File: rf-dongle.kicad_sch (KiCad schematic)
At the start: 0 parts

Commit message: add first draft of schematic
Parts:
- added C1, C17, C18, C2: 12pF, Capacitor_SMD:C_0402_1005Metric, symbol Device:C
- added C10, C13, C22: N.C., Capacitor_SMD:C_0402_1005Metric, symbol Device:C
- added C11: 100pF, Capacitor_SMD:C_0402_1005Metric, symbol Device:C
- added C12, C23, C5, C7, C8: 100nF, Capacitor_SMD:C_0402_1005Metric, symbol Device:C
- added C14, C15: 1.0µF, Capacitor_SMD:C_0603_1608Metric, symbol Device:C
- added C19, C20, C6: 4.7µF, Capacitor_SMD:C_0603_1608Metric, symbol Device:C
- added C3: 0.8pF, Capacitor_SMD:C_0402_1005Metric, symbol Device:C
- added C4: 0.5pF, Capacitor_SMD:C_0402_1005Metric, symbol Device:C
- added C9: 820pF, Capacitor_SMD:C_0402_1005Metric, symbol Device:C
- added D1: PRTR5V0U2X, Package_TO_SOT_SMD:SOT-143, symbol Power_Protection:PRTR5V0U2X
- added D2, D3: LED, LED_SMD:LED_0402_1005Metric, symbol Device:LED
- added J1: USB_A, 1_Library:PCB_USB_connector, symbol Connector:USB_A
- added J3: SWD, Connector_PinSocket_1.00mm:PinSocket_1x03_P1.00mm_Vertical_SMD_Pin1Left, symbol Connector:Conn_01x03_Socket
- added J4: PWR, Connector_PinSocket_1.00mm:PinSocket_1x02_P1.00mm_Vertical_SMD_Pin1Left, symbol Connector:Conn_01x02_Socket
- added JP1: SolderJumper_2_Bridged, Jumper:SolderJumper-2_P1.3mm_Bridged_RoundedPad1.0x1.5mm, symbol Jumper:SolderJumper_2_Bridged
- added L1: 4.7nH, Inductor_SMD:L_0402_1005Metric, symbol Device:L
- added R1: 2R2, Resistor_SMD:R_0402_1005Metric, symbol Device:R
- added R2: 10k, Resistor_SMD:R_0402_1005Metric, symbol Device:R
- added R3, R4: 56, Resistor_SMD:R_0201_0603Metric, symbol Device:R
- added SW1: SW_Push, Button_Switch_SMD:SW_SPST_B3U-1000P, symbol Switch:SW_Push
- added SW2: SW_Push, Button_Switch_SMD:SW_Push_1P1T-SH_NO_CK_KMR2xxG, symbol Switch:SW_Push
- added U1: nRF52840-QIXX, Package_DFN_QFN:Nordic_AQFN-73-1EP_7x7mm_P0.5mm, symbol PCM_nordic-lib-kicad-nrf52:nRF52840-QIXX
- added X1: 32MHz, Crystal:Crystal_SMD_2016-4Pin_2.0x1.6mm, symbol Device:Crystal_GND24
- added X2: 32.768kHz, Crystal:Crystal_SMD_2012-2Pin_2.0x1.2mm, symbol Device:Crystal
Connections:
- new net: D2.1 (K), R3.2
- new net: JP1.2 (B), R2.1
- new net: C3.2, L1.1, U1.H23 (ANT)
- new net: D3.1 (K), R4.2
- new net BTN_1: SW2.2
- new net DEC1: C5.1, U1.C1 (DEC1)
- new net DEC2: C13.1, U1.A18 (DEC2)
- new net DEC3: C11.1, U1.D23 (DEC3)
- new net DEC4_6: C10.2, C15.2, U1.B5 (DEC4), U1.E24 (DEC6)
- new net DEC5: C9.2, U1.N24 (DEC5)
- new net DECUSB: C20.2, U1.AC5 (DECUSB)
- new net D_M: D1.2 (I/O1), J1.2 (D-), U1.AD4 (D-)
- new net D_P: D1.3 (I/O2), J1.3 (D+), U1.AD6 (D+)
- new net GND: C1.1, C10.1, C11.2, C12.1, C13.2, C14.1, C15.1, C17.1, C18.2, C19.1, C2.2, C20.1, C22.1, C23.1, C3.1, C4.1, C5.2, C6.1, C7.1, C8.1, C9.1, D1.1 (GND), J1.4 (GND), J3.3 (Pin_3), R3.1, R4.1, SW1.1, SW2.1, U1.B7 (VSS), U1.EP (VSS), U1.F23 (VSS_PA), X1.2, X1.4
- new net LED_1: D2.2 (A)
- new net LED_2: D3.2 (A)
- new net RESET: C23.2, R2.2, SW1.2, U1.AC13 (~{RESET})
- new net RF: C22.2, C4.2, L1.2
- new net SWDCLK: J4.2 (Pin_2), U1.AA24 (SWDCLK)
- new net SWDIO: J4.1 (Pin_1), U1.AC24 (SWDIO)
- new net VBUS: D1.4 (VCC), J1.1 (VBUS), J3.1 (Pin_1), R1.2
- new net VBUS_nRF: C19.2, R1.1, U1.AD2 (VBUS), U1.Y2 (VDDH)
- new net VEXT: C12.2, C14.2, C6.2, C7.2, C8.2, J3.2 (Pin_2), JP1.1 (A), U1.A22 (VDD), U1.AD14 (VDD), U1.AD23 (VDD), U1.B1 (VDD), U1.W1 (VDD)
- new net XC1: C1.2, U1.B24 (XC1), X1.1
- new net XC2: C2.1, U1.A23 (XC2), X1.3
- new net XL1: C17.2, U1.D2 (P0.00), X2.1
- new net XL2: C18.1, U1.F2 (P0.01), X2.2
- no-connect marks 0 -> 48
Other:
- note added: "Antenna"
- note added: "BOM: - nRF52840 module, E73-2G4M08S1C, 6.4306 EUR - 5v ESD protection, PRTR5V0U2X-HXY, 0.0371 EUR - Cap. 50v 12pF C0G 1%, GJM1555C1H120FB01D, 0.0293 EUR - Cap. 50v 100nF X7R 10%, GRM155R71H104KE14D, 0.0026 EUR - Cap. 25v 10nF X7R 10%, GRM155R71E103KA01D, 0.0014 EUR - Res. 62.5mW 2R2 1%, 0402WGF220KTCE, 0.0007 EUR - Res. 62.5mW 10k 1%, 0402WGF1002TCE, 0.0004 EUR - LED 20mA 35mcd 2V Yel., BL-HGE37A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"
- note added: "Configurable Button"
- note added: "Decoupling Capacitors"
- note added: "High Frequency Clock"
- note added: "LEDs"
- note added: "Low Frequency Clock"
- note added: "Most of the schematic is a direct copy of the reference schematic for the QFAA layout. The only exceptions are the LEDs, configurable button, programming pins and reset button."
- note added: "Not completely sure the pullup is needed, so adding a solder bridge to allow disconnecting it in case I'm wrong."
- note added: "Programming Pins"
- note added: "RF Dongle (based on nRF52840)"
- note added: "Reset Button"
- note added: "Reset pin can technically be configured to either reset on connect or disconnect, but it's pulled up on nRF52-DK and Dongle, so leaving it pulled up here as well."
- note added: "Resistor and decoupling capacitor values are copied from the nRF52-Dongle schematic."
- note added: "Shield left floating since it's grounded by the host."
- note added: "Should be placed as close as possible to the connector and the data lines. The nRF52-Dongle uses decoupling capacitors, but the datasheet says no external capacitors are needed, so leaving them out. Avoid connecting ground to a common ground point (ESD return should be separate from signal return)."
- note added: "Status LEDs."
- note added: "TODO: - [ ] Select components - [ ] Inductor - [ ] Capacitors - [ ] Resistor - [ ] Antenna (?) - [ ] Define pins for LEDs - [ ] Define pins for Button"
- note added: "The JTAG connector was taking too much surface area, so switched to including two headers with split power and signal for easier routing"
- note added: "USB connector"
- note added: "User configurable button (e.g. for pairing). GPIO pins have an internal 13k pull-up resistor, so one is not needed here. Also this is the same setup as the nRF52-DK"

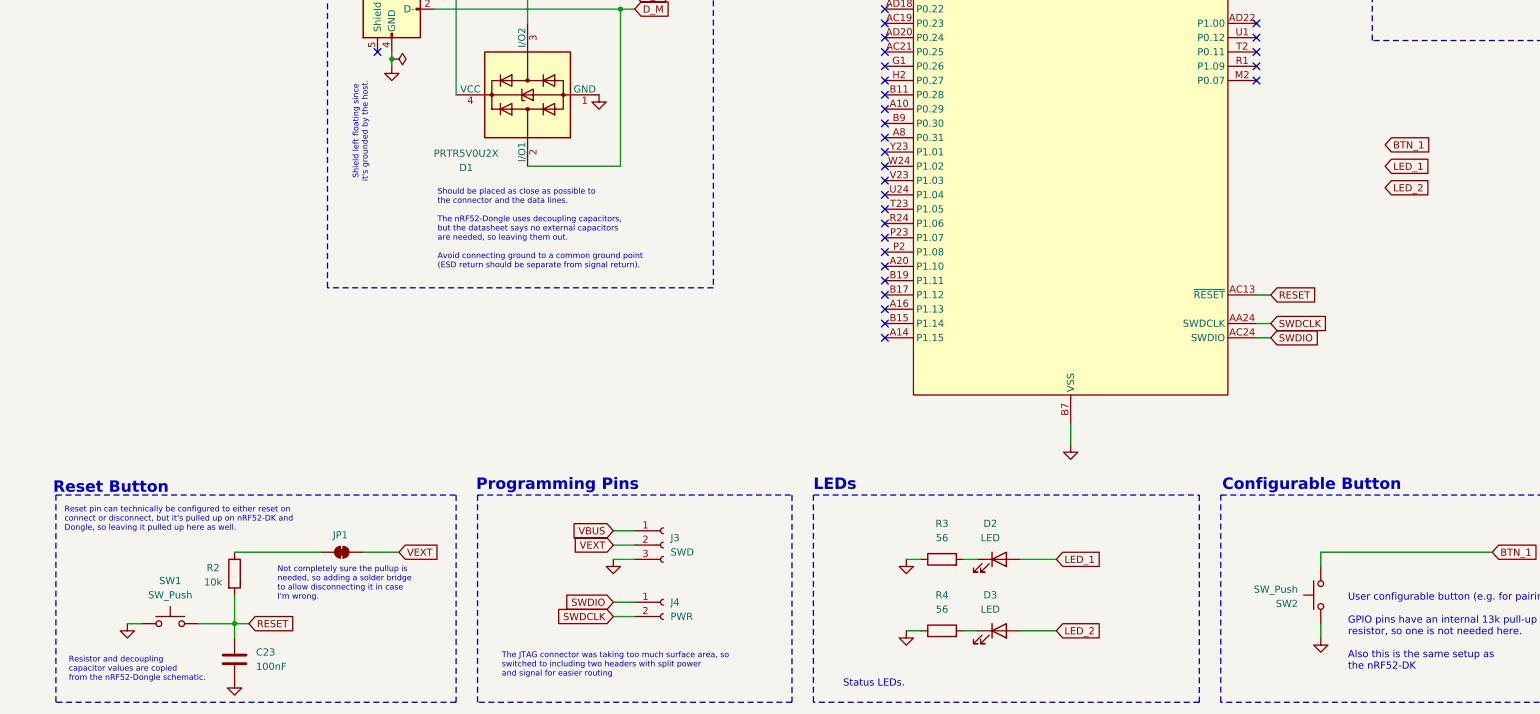
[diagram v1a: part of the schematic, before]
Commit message: add rough pcb layout
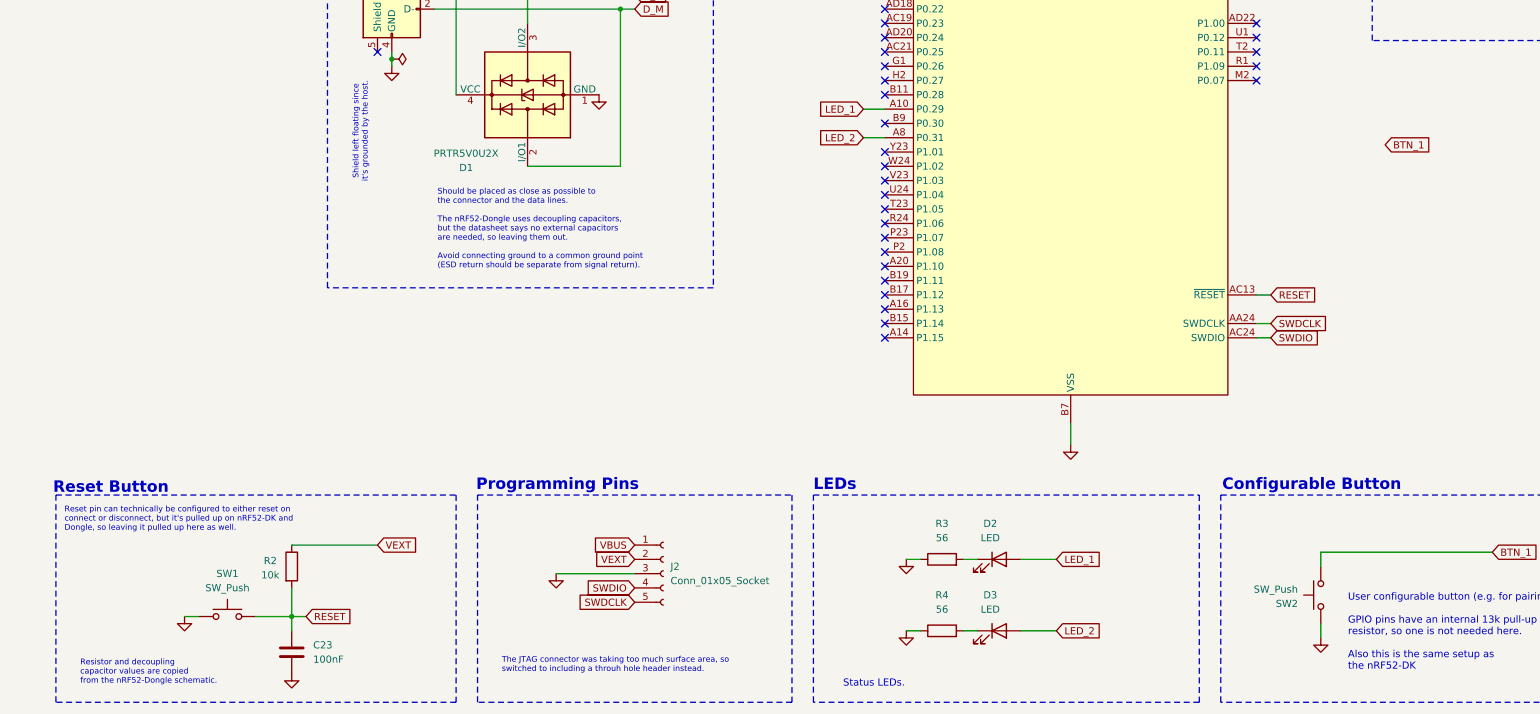
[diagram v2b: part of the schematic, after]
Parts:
- removed J3: SWD, Connector_PinSocket_1.00mm:PinSocket_1x03_P1.00mm_Vertical_SMD_Pin1Left, symbol Connector:Conn_01x03_Socket
- removed J4: PWR, Connector_PinSocket_1.00mm:PinSocket_1x02_P1.00mm_Vertical_SMD_Pin1Left, symbol Connector:Conn_01x02_Socket
- removed JP1: SolderJumper_2_Bridged, Jumper:SolderJumper-2_P1.3mm_Bridged_RoundedPad1.0x1.5mm, symbol Jumper:SolderJumper_2_Bridged
- added J2: Conn_01x05_Socket, Connector_PinHeader_1.00mm:PinHeader_1x05_P1.00mm_Vertical, symbol Connector:Conn_01x05_Socket
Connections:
- net GND: now also J2.3 (Pin_3)
- net LED_1: now also U1.A10 (P0.29)
- net LED_2: now also U1.A8 (P0.31)
- net SWDCLK: now also J2.5 (Pin_5)
- net SWDIO: now also J2.4 (Pin_4)
- net VBUS: now also J2.1 (Pin_1)
- net VEXT: now also R2.1, J2.2 (Pin_2)
- no-connect marks 48 -> 46
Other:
- note added: "The JTAG connector was taking too much surface area, so switched to including a throuh hole header instead."
- note removed: "Not completely sure the pullup is needed, so adding a solder bridge to allow disconnecting it in case I'm wrong."
- note removed: "The JTAG connector was taking too much surface area, so switched to including two headers with split power and signal for easier routing"
- moved on the sheet: C23, R2, SW1

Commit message: setup pcb stackup
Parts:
- removed C23: 100nF, Capacitor_SMD:C_0402_1005Metric, symbol Device:C
- added AE1: Antenna_Chip, Inductor_SMD:L_TDK_MLZ1608, symbol Device:Antenna_Chip
- added J3: TC2030, Connector:Tag-Connect_TC2030-IDC-NL_2x03_P1.27mm_Vertical, symbol Connector:TC2030
- added J4: TC2050-IDC-NL, Connector:Tag-Connect_TC2050-IDC-NL_2x05_P1.27mm_Vertical, symbol Connector:TC2050
- added JP1: SolderJumper_3_Bridged12, Jumper:SolderJumper-3_P1.3mm_Bridged2Bar12_RoundedPad1.0x1.5mm, symbol Jumper:SolderJumper_3_Bridged12
- added Z2: 3.9nH, Inductor_SMD:L_0402_1005Metric, symbol Device:L
- added Z3: N.C, Capacitor_SMD:C_0402_1005Metric, symbol Device:C
- J2: now not fitted
- SW2: footprint Button_Switch_SMD:SW_Push_1P1T-SH_NO_CK_KMR2xxG -> Button_Switch_SMD:SW_SPST_B3U-1000P
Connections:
- net GND: now also J3.1, J3.6, J4.3, J4.9, JP1.3 (B), Z3.1
- net RF: now also Z2.1
- net SWDCLK: now also J3.5, J4.4
- net SWDIO: now also J3.3, J4.2
- net VBUS: now also J3.2, JP1.1 (A)
- new net: AE1.1 (FEED), Z2.2, Z3.2
- new net: J4.5, JP1.2 (C)
- new net VDD_nRF: J3.4, J4.1
- no-connect marks 46 -> 51
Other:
- note added: "Antenna matching network, used to reduce noise from the antenna's output."
- note added: "BOM: - nRF52840 QIAA (aQFN), NRF52840-QIAA-R7, 3.3474 EUR - 5v ESD protection, PRTR5V0U2X-HXY, 0.0371 EUR ? Cap. 50v 12pF C0G 1%, GJM1555C1H120FB01D, 0.0293 EUR ? Cap. 50v 100nF X7R 10%, GRM155R71H104KE14D, 0.0026 EUR ? Cap. 25v 10nF X7R 10%, GRM155R71E103KA01D, 0.0014 EUR ? Res. 62.5mW 2R2 1%, 0402WGF220KTCE, 0.0007 EUR ? Res. 62.5mW 10k 1%, 0402WGF1002TCE, 0.0004 EUR - LED 20mA 35mcd 2V Yel., B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"
- note added: "In the current configuration pin 5 is 5v supplied by the debugger. If the debugger is not able to supply power to the DUT, cutting the connection 1-2 and soldering 2-3 on the solder bridge, will tie pin 5 to GND, requiring the device to be powered via VBUS instead."
- note added: "JTAG Connector (SWD)"
- note added: "Radio matching network, used to reduce noise from the transceiver's output (on the microcontroller side)."
- note added: "The RESET pin (10) is optional, since RESET can be triggered via SWD command."
- note removed: "BOM: - nRF52840 module, E73-2G4M08S1C, 6.4306 EUR - 5v ESD protection, PRTR5V0U2X-HXY, 0.0371 EUR - Cap. 50v 12pF C0G 1%, GJM1555C1H120FB01D, 0.0293 EUR - Cap. 50v 100nF X7R 10%, GRM155R71H104KE14D, 0.0026 EUR - Cap. 25v 10nF X7R 10%, GRM155R71E103KA01D, 0.0014 EUR - Res. 62.5mW 2R2 1%, 0402WGF220KTCE, 0.0007 EUR - Res. 62.5mW 10k 1%, 0402WGF1002TCE, 0.0004 EUR - LED 20mA 35mcd 2V Yel., BL-HGE37A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"
- moved on the sheet: C22, C3, C4, L1

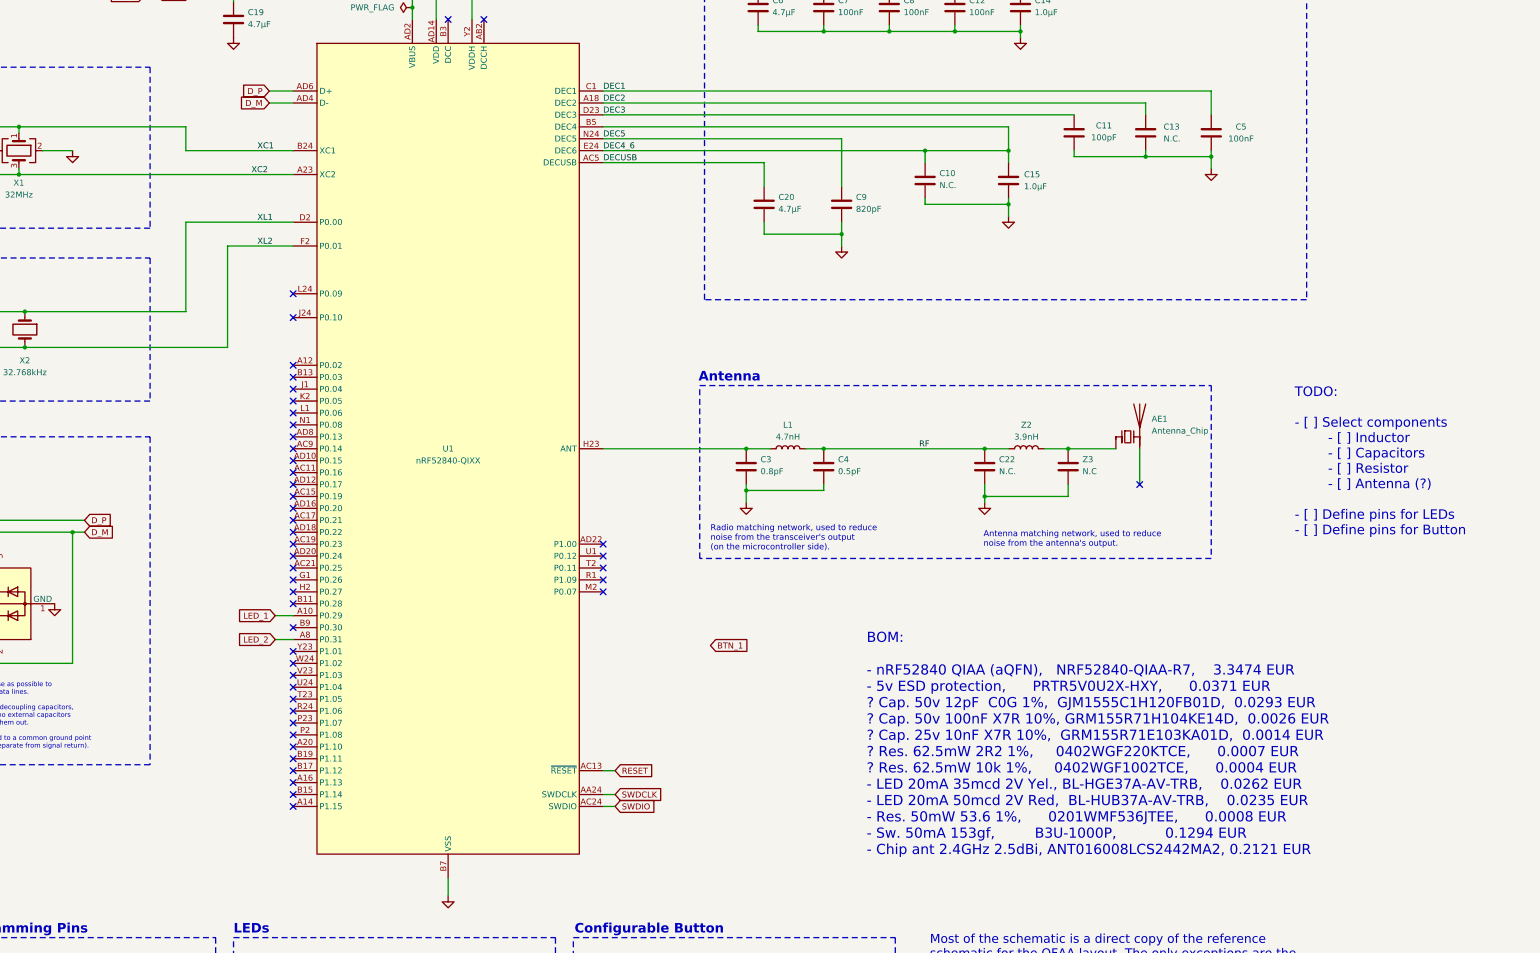
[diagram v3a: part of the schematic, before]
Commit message: setup constraints, first attempt at routing
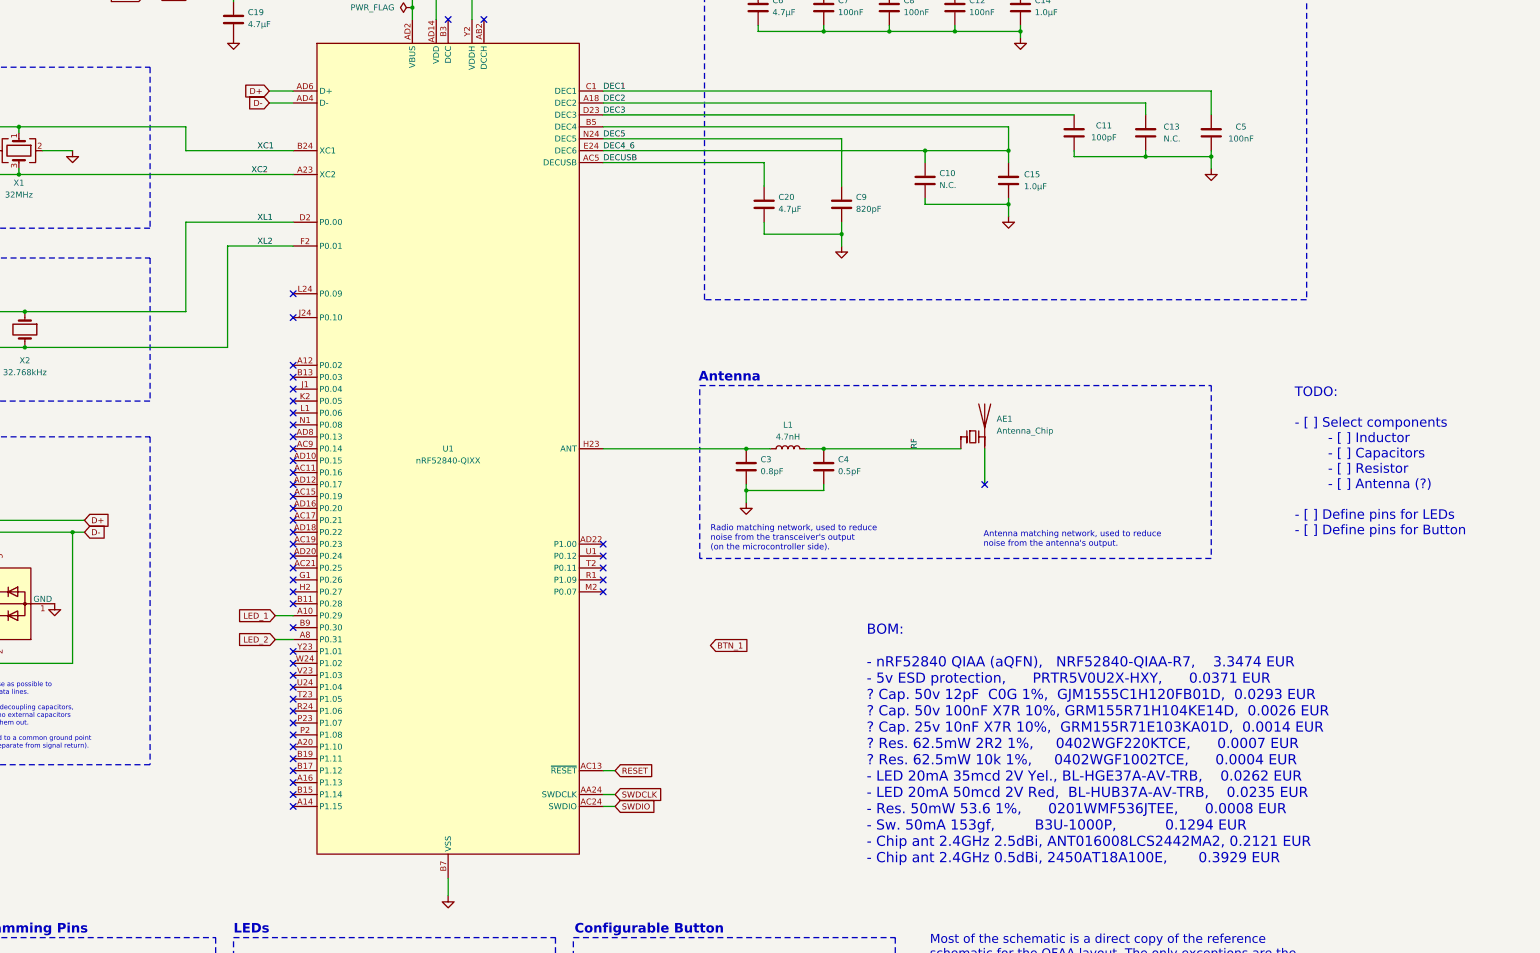
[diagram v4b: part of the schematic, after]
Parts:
- removed C22: N.C., Capacitor_SMD:C_0402_1005Metric, symbol Device:C
- removed Z2: 3.9nH, Inductor_SMD:L_0402_1005Metric, symbol Device:L
- removed Z3: N.C, Capacitor_SMD:C_0402_1005Metric, symbol Device:C
- AE1: footprint Inductor_SMD:L_TDK_MLZ1608 -> RF_Antenna:Johanson_2450AT18x100
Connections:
- net RF: now also AE1.1 (FEED)
- net D_M renamed D-
- net D_P renamed D+
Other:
- moved on the sheet: AE1

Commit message: second attempt at routing
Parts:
- removed J2: Conn_01x05_Socket, Connector_PinHeader_1.00mm:PinHeader_1x05_P1.00mm_Vertical, symbol Connector:Conn_01x05_Socket
- removed J4: TC2050-IDC-NL, Connector:Tag-Connect_TC2050-IDC-NL_2x05_P1.27mm_Vertical, symbol Connector:TC2050
- removed JP1: SolderJumper_3_Bridged12, Jumper:SolderJumper-3_P1.3mm_Bridged2Bar12_RoundedPad1.0x1.5mm, symbol Jumper:SolderJumper_3_Bridged12
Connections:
- net VDD_nRF is gone; now on net GND: J3.4
- net BTN_1: now also U1.A12 (P0.02)
- net GND: no longer J3.1
- net VEXT: now also J3.1
- net ANT: now reaches C3.2, L1.1, U1.H23 (ANT)
- no-connect marks 51 -> 46
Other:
- note added: "The pinout for the connector is custom to simplify routing."
- note removed: "In the current configuration pin 5 is 5v supplied by the debugger. If the debugger is not able to supply power to the DUT, cutting the connection 1-2 and soldering 2-3 on the solder bridge, will tie pin 5 to GND, requiring the device to be powered via VBUS instead."
- note removed: "Programming Pins"
- note removed: "The JTAG connector was taking too much surface area, so switched to including a throuh hole header instead."
- note removed: "The RESET pin (10) is optional, since RESET can be triggered via SWD command."
- moved on the sheet: AE1, C4, J3, L1

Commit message: before new programming pins
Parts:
- added H1: VBUS, TestPoint:TestPoint_THTPad_D1.0mm_Drill0.5mm, symbol Mechanical:MountingHole_Pad
- added H2: VEXT, TestPoint:TestPoint_THTPad_D1.0mm_Drill0.5mm, symbol Mechanical:MountingHole_Pad
- added H3: SWDIO, TestPoint:TestPoint_THTPad_D1.0mm_Drill0.5mm, symbol Mechanical:MountingHole_Pad
- added H4: SWDCLK, TestPoint:TestPoint_THTPad_D1.0mm_Drill0.5mm, symbol Mechanical:MountingHole_Pad
- added H5: GND, TestPoint:TestPoint_THTPad_D1.0mm_Drill0.5mm, symbol Mechanical:MountingHole_Pad
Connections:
- net GND: now also H5.1
- net SWDCLK: now also H4.1
- net SWDIO: now also H3.1
- net VBUS: now also H1.1
- net VEXT: now also H2.1
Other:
- moved on the sheet: J3
